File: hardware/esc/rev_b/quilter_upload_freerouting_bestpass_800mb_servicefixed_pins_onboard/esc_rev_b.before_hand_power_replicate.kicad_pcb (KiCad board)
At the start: 6 copper layers, 170 x 172.2 mm, 681 parts, among them J1101 FUSED_BATTERY_TAP, J1102 MOTOR_PHASES, J1103 LOCAL_SWD, J1201 FUSED_BATTERY_TAP, J1202 MOTOR_PHASES, J1203 LOCAL_SWD, J1301 FUSED_BATTERY_TAP, J1302 MOTOR_PHASES, J1303 LOCAL_SWD, J1401 FUSED_BATTERY_TAP, J1402 MOTOR_PHASES, J1403 LOCAL_SWD, J1501 FUSED_BATTERY_TAP, J1502 MOTOR_PHASES, J1503 LOCAL_SWD, J1601 FUSED_BATTERY_TAP, J1602 MOTOR_PHASES, J1603 LOCAL_SWD, J201 ESC_SWD, J202 CTRL_USB_C, J203 MOTOR_DFU_USB_C, J701 AUX_BATTERY, J702 FLIGHT_CAN_POWER, Q1101 IPTC014N10NM5, Q1102 IPTC014N10NM5, Q1103 IPTC014N10NM5, Q1104 IPTC014N10NM5, Q1105 IPTC014N10NM5, Q1106 IPTC014N10NM5, Q1201 IPTC014N10NM5, Q1202 IPTC014N10NM5, Q1203 IPTC014N10NM5, Q1204 IPTC014N10NM5, Q1205 IPTC014N10NM5, Q1206 IPTC014N10NM5, Q1301 IPTC014N10NM5, Q1302 IPTC014N10NM5, Q1303 IPTC014N10NM5, Q1304 IPTC014N10NM5, Q1305 IPTC014N10NM5, Q1306 IPTC014N10NM5, Q1401 IPTC014N10NM5, Q1402 IPTC014N10NM5, Q1403 IPTC014N10NM5, Q1404 IPTC014N10NM5, Q1405 IPTC014N10NM5, Q1406 IPTC014N10NM5, Q1501 IPTC014N10NM5, Q1502 IPTC014N10NM5, Q1503 IPTC014N10NM5, Q1504 IPTC014N10NM5, Q1505 IPTC014N10NM5, Q1506 IPTC014N10NM5, Q1601 IPTC014N10NM5, Q1602 IPTC014N10NM5, Q1603 IPTC014N10NM5, Q1604 IPTC014N10NM5, Q1605 IPTC014N10NM5, Q1606 IPTC014N10NM5, SW201 6-WAY ACTIVE-LOW SELECTOR, U1101 DRV8353SRTAR, U1102 STM32G431CBT6, U1103 ISO6731FDWR, U1104 TPS70933DBVR, U1105 INA296A2IDR, U1106 SN74LVC1G08DBVR, U1107 USBLC6-2SC6, U1201 DRV8353SRTAR, U1202 STM32G431CBT6, U1203 ISO6731FDWR, U1204 TPS70933DBVR, U1205 INA296A2IDR, U1206 SN74LVC1G08DBVR, U1207 USBLC6-2SC6, U1301 DRV8353SRTAR, U1302 STM32G431CBT6, U1303 ISO6731FDWR, U1304 TPS70933DBVR, U1305 INA296A2IDR, U1306 SN74LVC1G08DBVR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

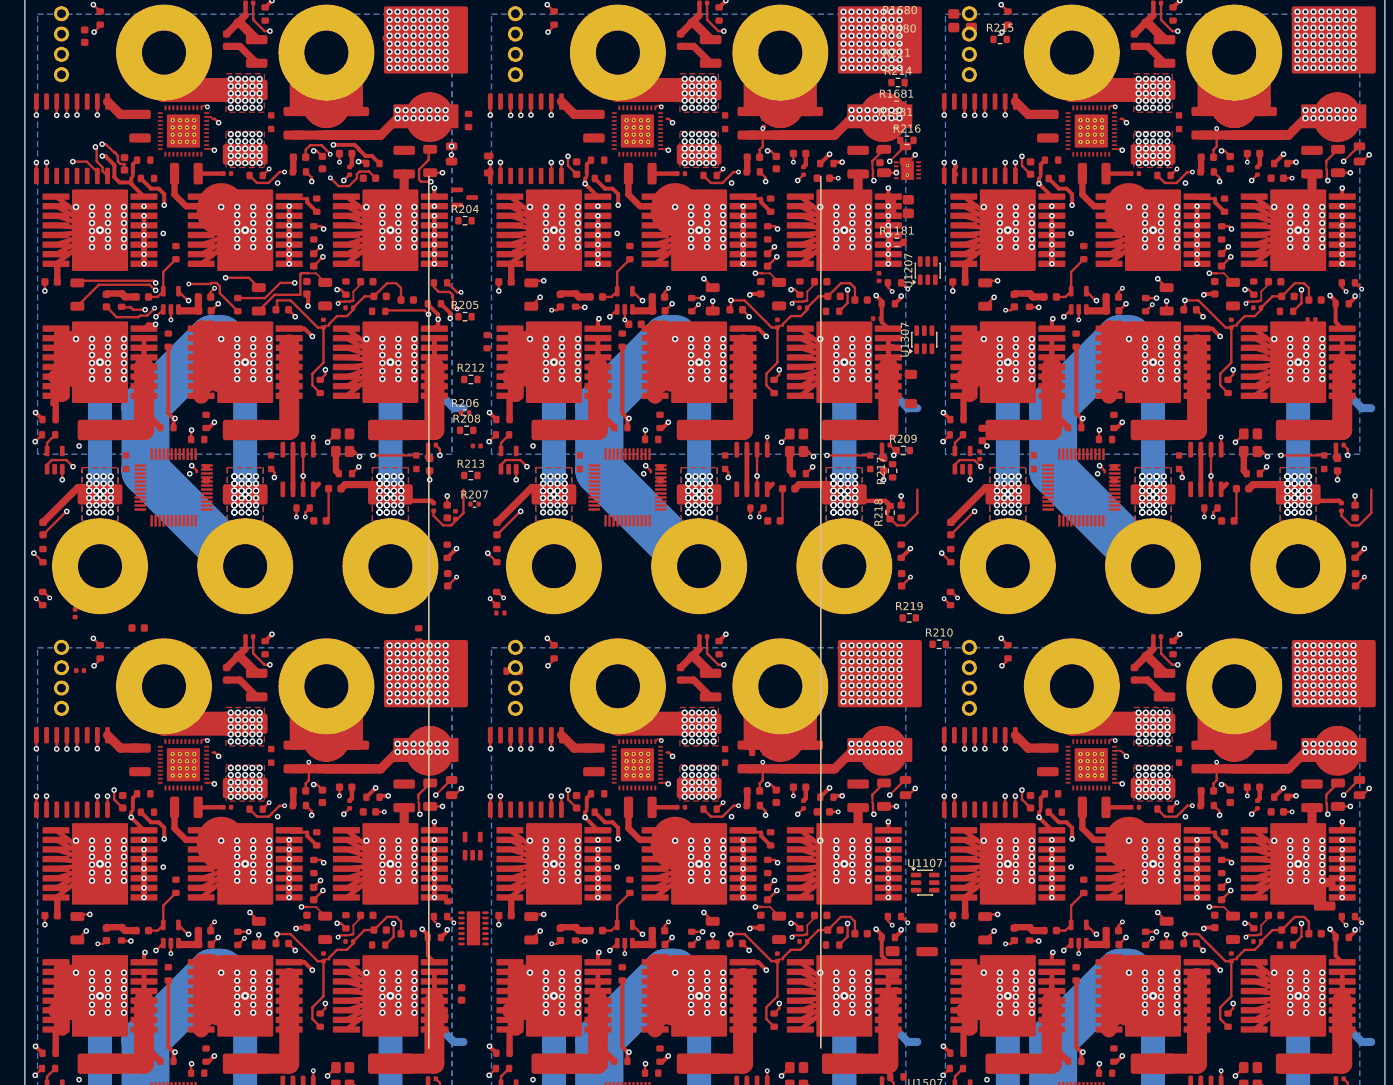
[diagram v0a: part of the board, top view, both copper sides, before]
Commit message: esc: replicate hand-routed power copper and free main diff pairs
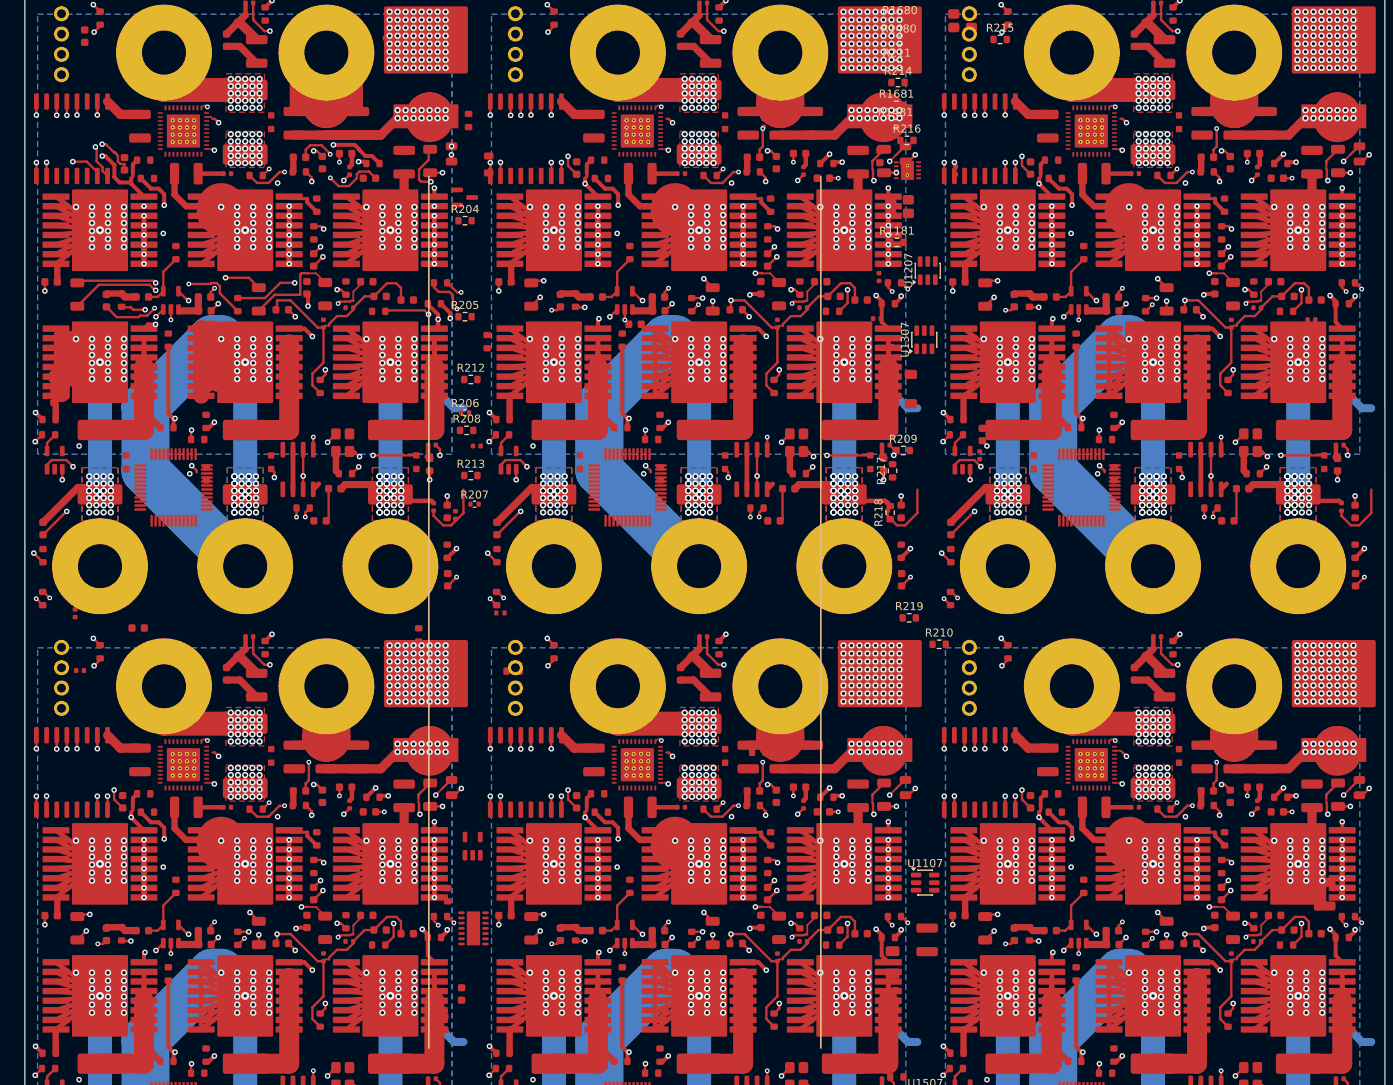
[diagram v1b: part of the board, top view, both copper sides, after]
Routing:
- net /M4_BATP: track 311.8 -> 225.8 mm
- net /M5_BATP: track 311.8 -> 225.8 mm
- net /M3_BATP: track 311.8 -> 225.8 mm
- net /M2_BATP: track 311.8 -> 225.8 mm
- net /M6_BATP: track 311.8 -> 225.8 mm
- net /M5_PHASE_A: track 184.2 -> 131.8 mm
- net /M4_PHASE_A: track 184.2 -> 131.8 mm
- net /M3_PHASE_A: track 184.2 -> 131.8 mm
- net /M6_PHASE_A: track 184.2 -> 131.8 mm
- net /M2_PHASE_A: track 184.2 -> 131.8 mm
- net /M3_PHASE_B: track 197.0 -> 147.3 mm
- net /M6_PHASE_B: track 197.0 -> 147.3 mm
- net /M5_PHASE_B: track 197.0 -> 147.3 mm
- net /M4_PHASE_B: track 197.0 -> 147.3 mm
- net /M2_PHASE_B: track 197.0 -> 147.3 mm
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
